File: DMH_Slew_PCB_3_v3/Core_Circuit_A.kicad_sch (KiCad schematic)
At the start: 60 parts, among them J1 TS_Jack_6.35mm_Sw, J11 Conn_02x03_Top_Bottom, J12 Conn_02x06_Top_Bottom, J13 Conn_02x03_Top_Bottom, J14 Conn_02x03_Top_Bottom, J15 Conn_02x06_Top_Bottom, J16 Conn_02x03_Top_Bottom, J17 Conn_01x08, J18 Conn_01x08, J19 Conn_01x08, J2 TS_Jack_6.35mm_Sw, J20 Conn_01x08, J3 TS_Jack_6.35mm_Sw, Q1 BC548, Q2 BC548, Q3 BC558, Q4 BC558, SW1 SW_DPDT_3way, SW2 SW_DPDT, SW3 SPDT_OnOffOn, U1 TL074, U2 TL074

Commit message: PCB 3 comp placement done
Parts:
- Q1, Q2, Q3, Q4: footprint Package_TO_SOT_THT:TO-92_Inline -> Package_TO_SOT_THT:TO-92L_Inline_Wide
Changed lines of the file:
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@@
 			)
 		)
-		(property "Footprint" "Package_TO_SOT_THT:TO-92_Inline"
+		(property "Footprint" "Package_TO_SOT_THT:TO-92L_Inline_Wide"
 			(at 226.695 168.91 0)
 			(effects
@@
 			)
 		)
-		(property "Footprint" "Package_TO_SOT_THT:TO-92_Inline"
+		(property "Footprint" "Package_TO_SOT_THT:TO-92L_Inline_Wide"
 			(at 226.695 161.29 0)
 			(effects
@@
 			)
 		)
-		(property "Footprint" "Package_TO_SOT_THT:TO-92_Inline"
+		(property "Footprint" "Package_TO_SOT_THT:TO-92L_Inline_Wide"
 			(at 205.105 161.29 0)
 			(effects
@@
 			)
 		)
-		(property "Footprint" "Package_TO_SOT_THT:TO-92_Inline"
+		(property "Footprint" "Package_TO_SOT_THT:TO-92L_Inline_Wide"
 			(at 205.105 168.91 0)
 			(effects

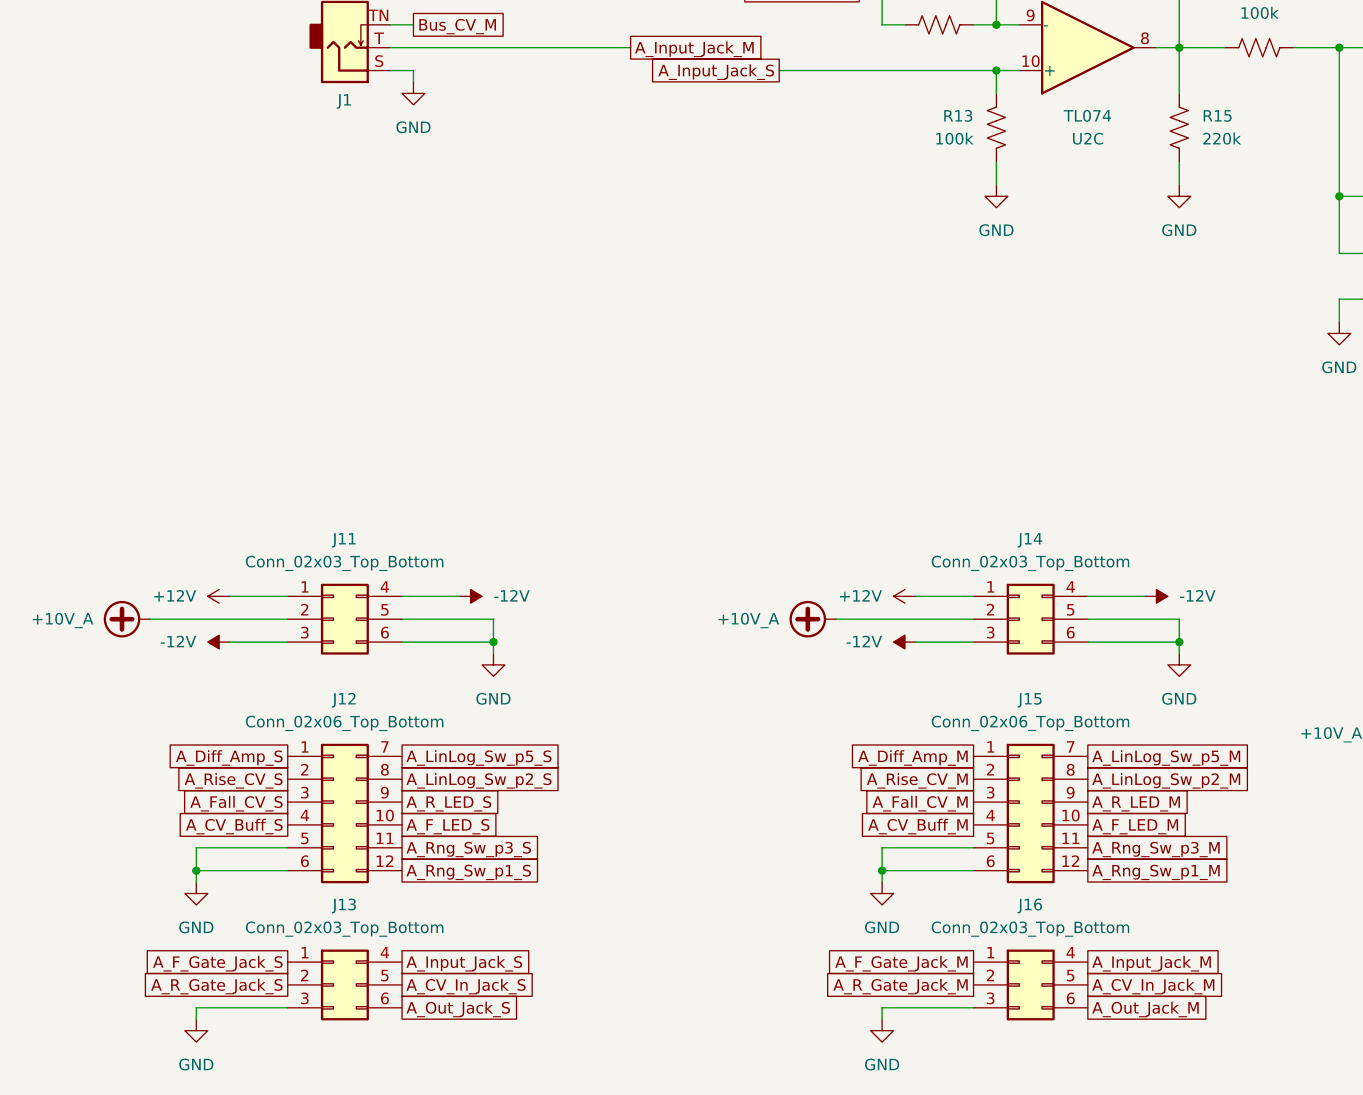
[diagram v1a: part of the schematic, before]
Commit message: Exposed loopback resistor to submodule connector
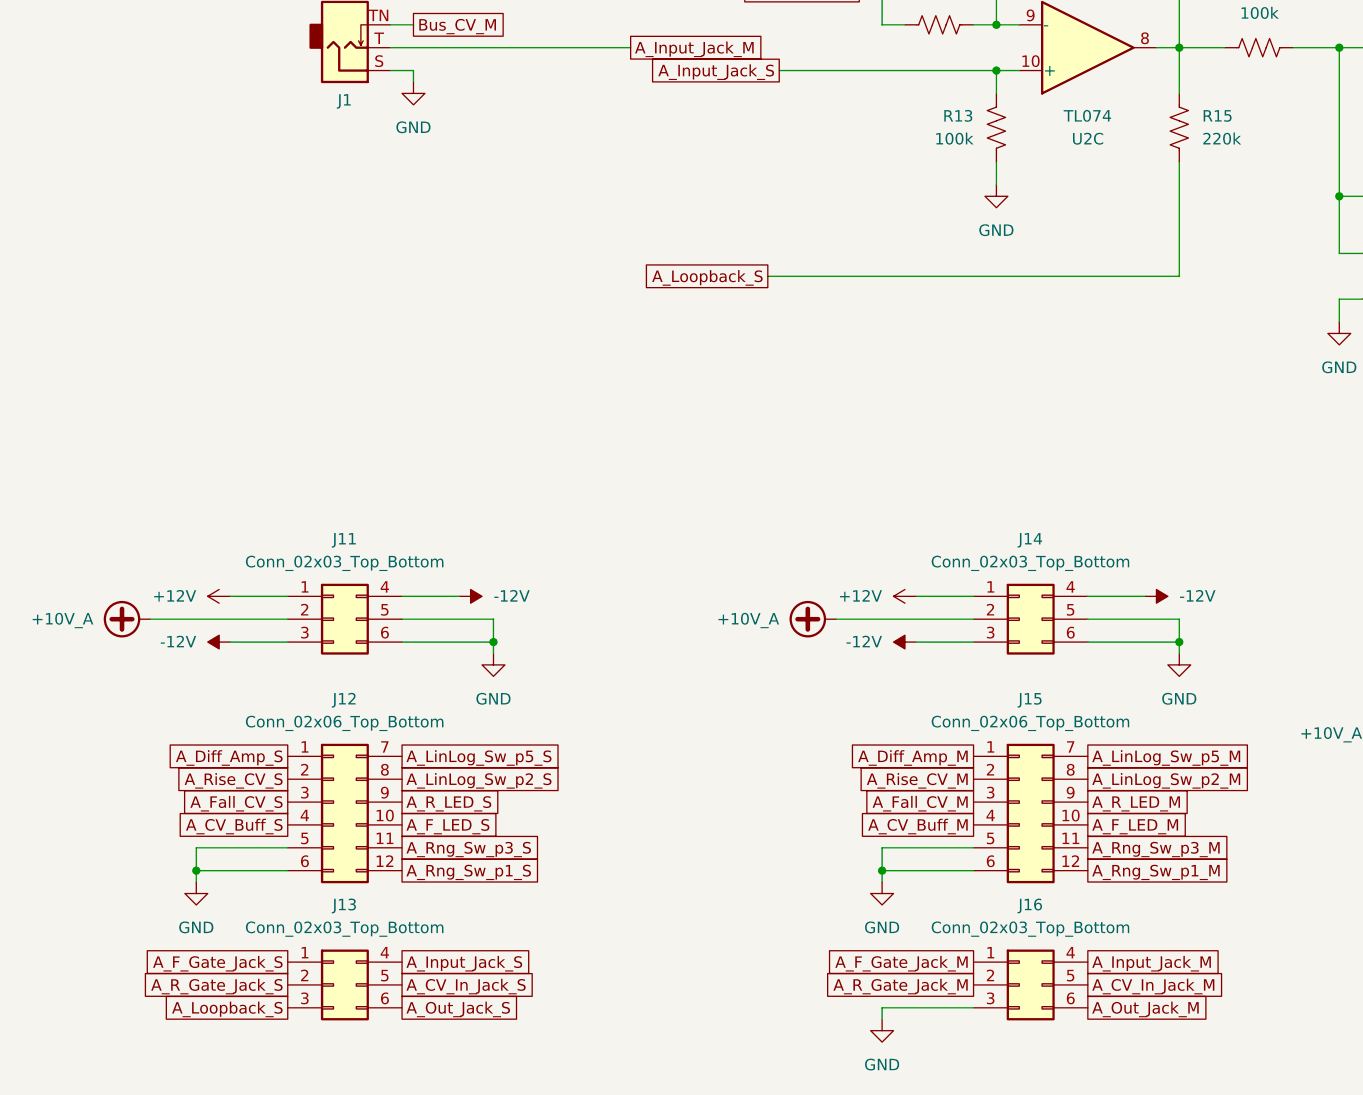
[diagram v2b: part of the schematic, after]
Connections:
- net GND: no longer J13.3 (Pin_3), R15.2
- new net A_Loopback_S: J13.3 (Pin_3), R15.2
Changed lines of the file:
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@@
 	(wire
 		(pts
-			(xy 284.48 195.58) (xy 279.4 195.58)
+			(xy 97.79 190.5) (xy 143.51 190.5)
 		)
 		(stroke
@@
 	(wire
 		(pts
-			(xy 165.1 97.79) (xy 167.64 97.79)
+			(xy 284.48 195.58) (xy 279.4 195.58)
 		)
 		(stroke
@@
 	(wire
 		(pts
-			(xy 342.9 87.63) (xy 349.25 87.63)
+			(xy 165.1 97.79) (xy 167.64 97.79)
 		)
 		(stroke
@@
 	(wire
 		(pts
-			(xy 393.7 226.06) (xy 393.7 228.6)
+			(xy 342.9 87.63) (xy 349.25 87.63)
 		)
 		(stroke
@@
 	(wire
 		(pts
-			(xy 275.59 67.31) (xy 266.7 67.31)
+			(xy 393.7 226.06) (xy 393.7 228.6)
 		)
 		(stroke
@@
 	(wire
 		(pts
-			(xy 143.51 177.8) (xy 143.51 180.34)
+			(xy 275.59 67.31) (xy 266.7 67.31)
 		)
 		(stroke
@@
 	(wire
 		(pts
-			(xy 44.45 271.78) (xy 34.29 271.78)
-		)
-		(stroke
-			(width 0)
-			(type default)
-		)
-	)
-	(wire
-		(pts
 			(xy 167.64 104.14) (xy 167.64 97.79)
 		)
@@
 	(wire
 		(pts
+			(xy 143.51 177.8) (xy 143.51 190.5)
+		)
+		(stroke
+			(width 0)
+			(type default)
+		)
+	)
+	(wire
+		(pts
 			(xy 384.81 80.01) (xy 387.35 80.01)
 		)
@@
 	(wire
 		(pts
-			(xy 34.29 271.78) (xy 34.29 273.05)
-		)
-		(stroke
-			(width 0)
-			(type default)
-		)
-	)
-	(wire
-		(pts
 			(xy 114.3 226.06) (xy 120.65 226.06)
 		)
@@
 		)
 	)
+	(global_label "A_Loopback_S"
+		(shape passive)
+		(at 97.79 190.5 180)
+		(fields_autoplaced yes)
+		(effects
+			(font
+				(size 1.27 1.27)
+			)
+			(justify right)
+		)
+		(property "Intersheetrefs" "${INTERSHEET_REFS}"
+			(at 82.793 190.5 0)
+			(effects
+				(font
+					(size 1.27 1.27)
+				)
+				(justify right)
+				(hide yes)
+			)
+		)
+	)
 	(global_label "A_Input_Jack_S"
 		(shape passive)
@@
 		)
 	)
+	(global_label "A_Loopback_S"
+		(shape passive)
+		(at 44.45 271.78 180)
+		(fields_autoplaced yes)
+		(effects
+			(font
+				(size 1.27 1.27)
+			)
+			(justify right)
+		)
+		(property "Intersheetrefs" "${INTERSHEET_REFS}"
+			(at 29.453 271.78 0)
+			(effects
+				(font
+					(size 1.27 1.27)
+				)
+				(justify right)
+				(hide yes)
+			)
+		)
+	)
 	(global_label "A_Rng_Sw_p3_M"
 		(shape passive)
@@
 		(polyline
 			(pts
-				(xy 44.45 152.4) (xy 78.74 152.4) (xy 78.74 177.8) (xy 44.45 177.8)
+				(xy 45.085 152.4) (xy 79.375 152.4) (xy 79.375 199.39) (xy 45.085 199.39)
 			)
 			(stroke
@@
 		(length 2.54)
 		(shape round)
-		(at 44.45 152.4 0)
+		(at 45.72 152.4 0)
 		(fields_autoplaced yes)
 		(effects
@@
 		)
 		(property "Component Class" "Main PCB"
-			(at 45.1485 149.86 0)
+			(at 46.4185 149.86 0)
 			(effects
 				(font
@@
 	(symbol
 		(lib_id "power:GND")
-		(at 143.51 180.34 0)
-		(unit 1)
-		(exclude_from_sim no)
-		(in_bom yes)
-		(on_board yes)
-		(dnp no)
-		(fields_autoplaced yes)
-		(property "Reference" "#PWR022"
-			(at 143.51 186.69 0)
-			(effects
-				(font
-					(size 1.27 1.27)
-				)
-				(hide yes)
-			)
-		)
-		(property "Value" "GND"
-			(at 143.51 185.42 0)
-			(effects
-				(font
-					(size 1.27 1.27)
-				)
-			)
-		)
-		(property "Footprint" ""
-			(at 143.51 180.34 0)
-			(effects
-				(font
-					(size 1.27 1.27)
-				)
-				(hide yes)
-			)
-		)
-		(property "Datasheet" ""
-			(at 143.51 180.34 0)
-			(effects
-				(font
-					(size 1.27 1.27)
-				)
-				(hide yes)
-			)
-		)
-		(property "Description" "Power symbol creates a global label with name \"GND\" , ground"
-			(at 143.51 180.34 0)
-			(effects
-				(font
-					(size 1.27 1.27)
-				)
-				(hide yes)
-			)
-		)
-		(pin "1"
-		)
-		(instances
-			(project "DMH_Slew_PCB_1_v3"
-				(path "/58f4306d-5387-4983-bb08-41a2313fd315/7ad2d702-dfb7-4d49-a82d-34430dd5948f"
-					(reference "#PWR022")
-					(unit 1)
-				)
-			)
-		)
-	)
-	(symbol
-		(lib_id "power:GND")
 		(at 44.45 86.36 0)
 		(unit 1)
@@
 					(unit 1)
 				)
-			)
-		)
-	)
-	(symbol
-		(lib_id "power:GND")
-		(at 34.29 273.05 0)
-		(mirror y)
-		(unit 1)
-		(exclude_from_sim no)
-		(in_bom yes)
-		(on_board yes)
-		(dnp no)
-		(fields_autoplaced yes)
-		(property "Reference" "#PWR0101"
-			(at 34.29 279.4 0)
-			(effects
-				(font
-					(size 1.27 1.27)
-				)
-				(hide yes)
-			)
-		)
-		(property "Value" "GND"
-			(at 34.29 278.13 0)
-			(effects
-				(font
-					(size 1.27 1.27)
-				)
-			)
-		)
-		(property "Footprint" ""
-			(at 34.29 273.05 0)
-			(effects
-				(font
-					(size 1.27 1.27)
-				)
-				(hide yes)
-			)
-		)
-		(property "Datasheet" ""
-			(at 34.29 273.05 0)
-			(effects
-				(font
-					(size 1.27 1.27)
-				)
-				(hide yes)
-			)
-		)
-		(property "Description" "Power symbol creates a global label with name \"GND\" , ground"
-			(at 34.29 273.05 0)
-			(effects
-				(font
-					(size 1.27 1.27)
-				)
-				(hide yes)
-			)
-		)
-		(pin "1"
-		)
-		(instances
-			(project "DMH_Slew_PCB_1_v3"
-				(path "/58f4306d-5387-4983-bb08-41a2313fd315/7ad2d702-dfb7-4d49-a82d-34430dd5948f"
-					(reference "#PWR0101")
-					(unit 1)
-				)

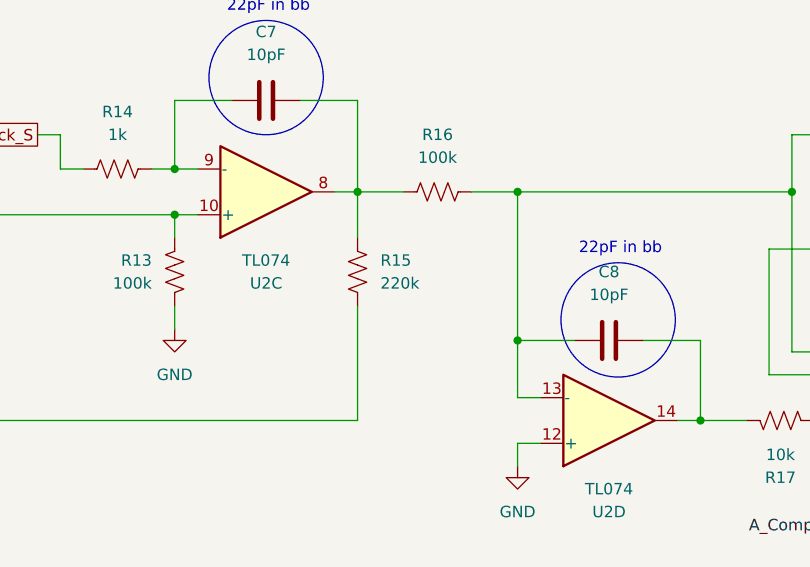
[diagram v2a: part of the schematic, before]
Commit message: Changed loopback resistor to 82k
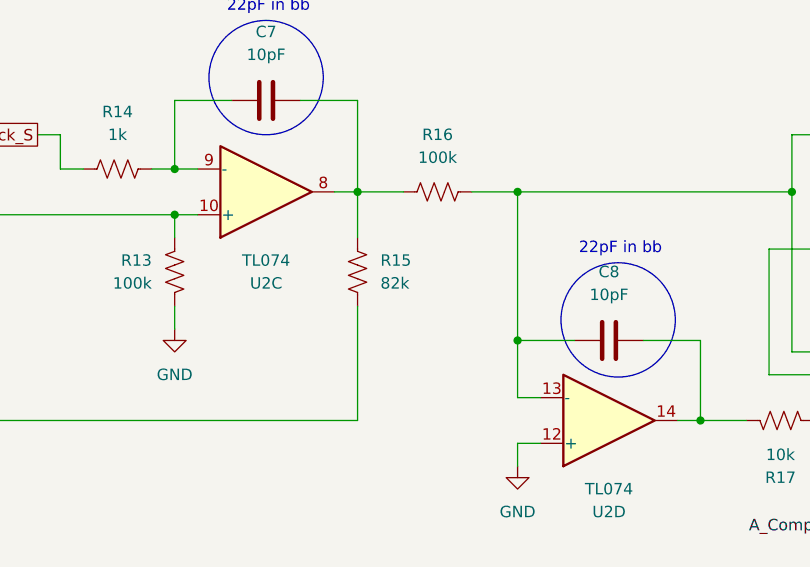
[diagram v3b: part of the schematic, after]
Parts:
- R15: value 220k -> 82k
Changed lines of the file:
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@@
 			)
 		)
-		(property "Value" "220k"
+		(property "Value" "82k"
 			(at 146.05 175.2599 0)
 			(effects
